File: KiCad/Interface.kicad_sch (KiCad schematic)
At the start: 30 parts, among them U14 SN65HVDA540, U15 SN65HVDA540, U16 LTC6820

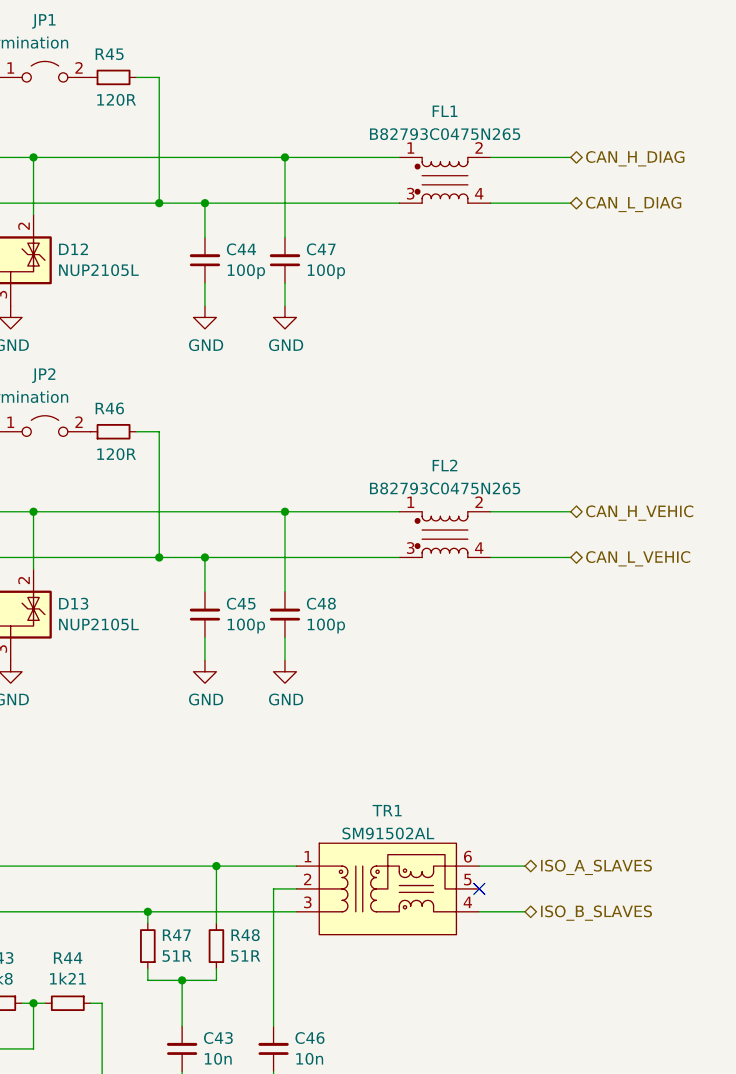
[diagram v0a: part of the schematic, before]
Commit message: Port to Kicad 7, small changes in auto-reset feature
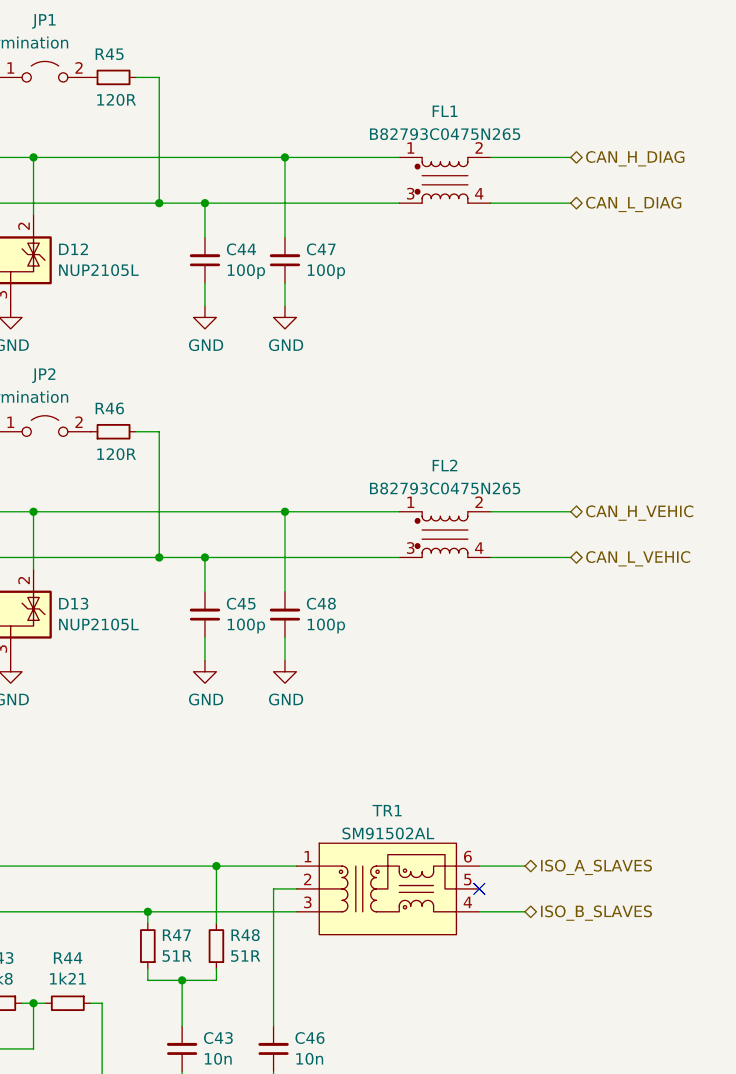
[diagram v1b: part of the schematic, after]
